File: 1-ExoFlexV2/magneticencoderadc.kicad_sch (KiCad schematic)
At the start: 72 parts, among them J55 Jumper, J56 Jumper, J58 Jumper, J59 Jumper, J66 Jumper, J67 Jumper, U17 OP_AMP2, U18 OP_AMP2, U19 OP_AMP2, U23 OP_AMP2, U24 OP_AMP2, U31 OP_AMP2

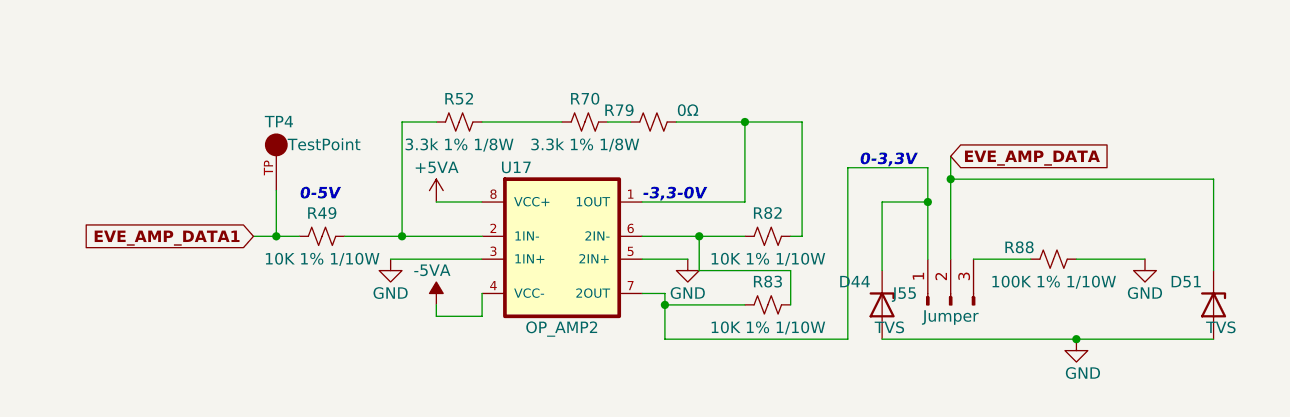
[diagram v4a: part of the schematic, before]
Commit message: Analyse Post-PMC
-Modification du footprint du régulateur de tension
- Inversion des condos et diode sur les tensions négative
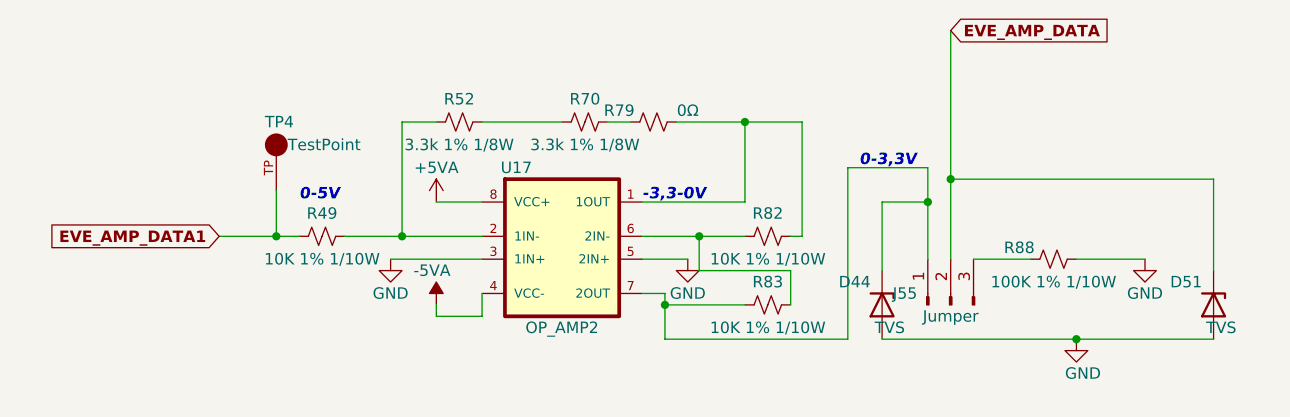
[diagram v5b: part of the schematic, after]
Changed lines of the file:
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@@
     (stroke (width 0) (type default) (color 0 0 0 0))
   )
-  (wire (pts (xy 111.76 34.29) (xy 111.76 31.75))
+  (wire (pts (xy 111.76 34.29) (xy 111.76 17.78))
     (stroke (width 0) (type default) (color 0 0 0 0))
   )
@@
     (stroke (width 0) (type default) (color 0 0 0 0))
   )
-  (wire (pts (xy 34.29 40.64) (xy 36.83 40.64))
+  (wire (pts (xy 30.48 40.64) (xy 36.83 40.64))
     (stroke (width 0) (type default) (color 0 0 0 0))
   )
@@
     (effects (font (size 1.27 1.27) (thickness 0.254) bold italic) (justify left bottom))
   )
-  (global_label "EVE_AMP_DATA" (shape input) (at 111.76 31.75 0) (fields_autoplaced)
+  (global_label "EVE_AMP_DATA" (shape input) (at 111.76 17.78 0) (fields_autoplaced)
     (effects (font (size 1.27 1.27) bold) (justify left))
-    (property "Intersheet References" "${INTERSHEET_REFS}" (id 0) (at 128.1007 31.623 0)
+    (property "Intersheet References" "${INTERSHEET_REFS}" (id 0) (at 128.1007 17.653 0)
       (effects (font (size 1.27 1.27) bold) (justify left) hide)
     )
@@
     )
   )
-  (global_label "EVE_AMP_DATA1" (shape input) (at 34.29 40.64 180) (fields_autoplaced)
+  (global_label "EVE_AMP_DATA1" (shape input) (at 30.48 40.64 180) (fields_autoplaced)
     (effects (font (size 1.27 1.27) bold) (justify right))
-    (property "Intersheet References" "${INTERSHEET_REFS}" (id 0) (at 16.7398 40.513 0)
+    (property "Intersheet References" "${INTERSHEET_REFS}" (id 0) (at 12.9298 40.513 0)
       (effects (font (size 1.27 1.27) bold) (justify right) hide)
     )
